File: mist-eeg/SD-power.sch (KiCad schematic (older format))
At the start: 14 parts, among them U8 TPS63070

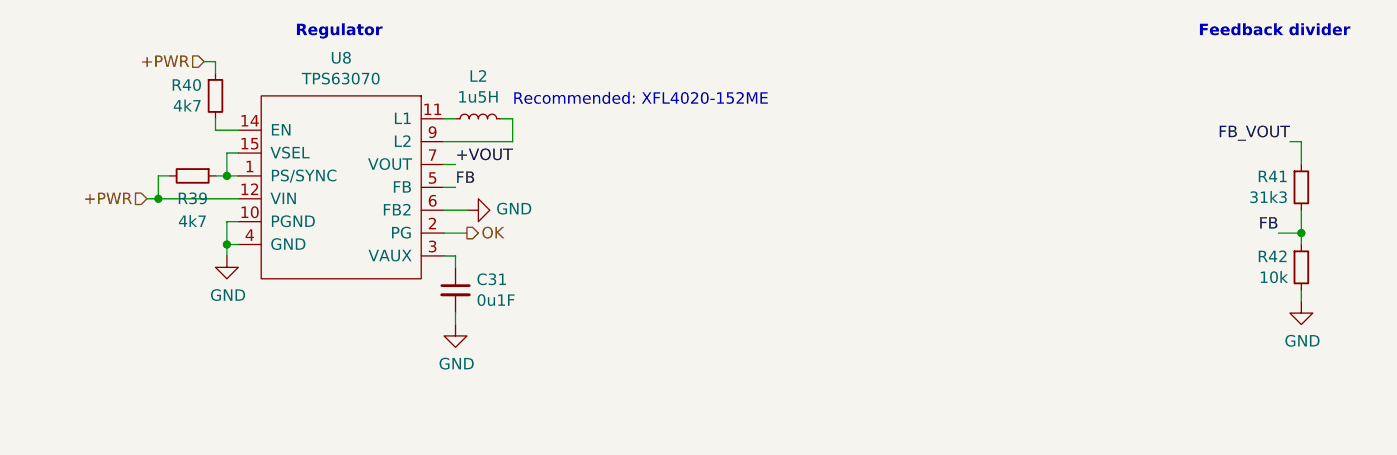
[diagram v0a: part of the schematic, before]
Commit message: Finish schematic and create interface specifications
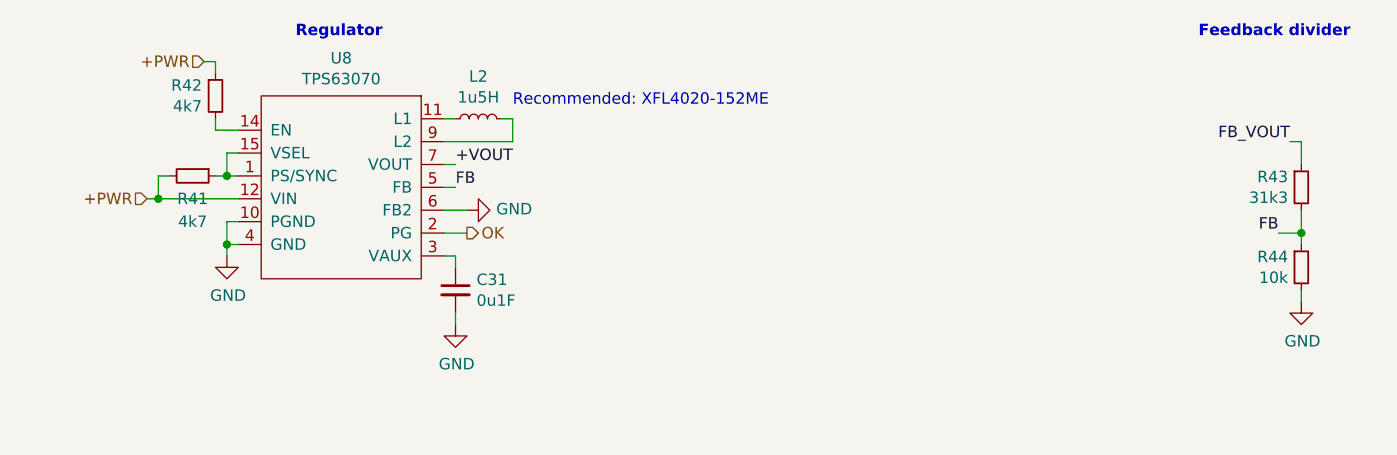
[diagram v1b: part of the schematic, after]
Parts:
- renumbered R39 to R41, R40 to R42, R41 to R43, R42 to R44
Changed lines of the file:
@@
 P 3750 2700
 AR Path="/609A79EB/60F89803/6135F6B6" Ref="R?"  Part="1"
-AR Path="/609A79EB/60FA92B1/6135F6B6" Ref="R39"  Part="1"
-F 0 "R39" V 3850 2700 50  0000 C CNN
+AR Path="/609A79EB/60FA92B1/6135F6B6" Ref="R41"  Part="1"
+F 0 "R41" V 3850 2700 50  0000 C CNN
 F 1 "4k7" V 3950 2700 50  0000 C CNN
 F 2 "Resistor_SMD:R_0201_0603Metric" H 3750 2700 50  0001 C CNN
@@
 P 8600 2750
 AR Path="/609A79EB/60F89803/6135F6F8" Ref="R?"  Part="1"
-AR Path="/609A79EB/60FA92B1/6135F6F8" Ref="R41"  Part="1"
-F 0 "R41" H 8542 2796 50  0000 R CNN
+AR Path="/609A79EB/60FA92B1/6135F6F8" Ref="R43"  Part="1"
+F 0 "R43" H 8542 2796 50  0000 R CNN
 F 1 "31k3" H 8542 2705 50  0000 R CNN
 F 2 "Resistor_SMD:R_0603_1608Metric" H 8600 2750 50  0001 C CNN
@@
 P 8600 3100
 AR Path="/609A79EB/60F89803/6135F6FE" Ref="R?"  Part="1"
-AR Path="/609A79EB/60FA92B1/6135F6FE" Ref="R42"  Part="1"
-F 0 "R42" H 8542 3146 50  0000 R CNN
+AR Path="/609A79EB/60FA92B1/6135F6FE" Ref="R44"  Part="1"
+F 0 "R44" H 8542 3146 50  0000 R CNN
 F 1 "10k" H 8542 3055 50  0000 R CNN
 F 2 "Resistor_SMD:R_0603_1608Metric" H 8600 3100 50  0001 C CNN
@@
 P 3850 2350
 AR Path="/609A79EB/60F89803/6135F719" Ref="R?"  Part="1"
-AR Path="/609A79EB/60FA92B1/6135F719" Ref="R40"  Part="1"
-F 0 "R40" H 3791 2396 50  0000 R CNN
+AR Path="/609A79EB/60FA92B1/6135F719" Ref="R42"  Part="1"
+F 0 "R42" H 3791 2396 50  0000 R CNN
 F 1 "4k7" H 3791 2305 50  0000 R CNN
 F 2 "Resistor_SMD:R_0201_0603Metric" H 3850 2350 50  0001 C CNN
@@
 P 2400 5100
 AR Path="/609A79EB/60F89803/6135F747" Ref="#PWR?"  Part="1"
-AR Path="/609A79EB/60FA92B1/6135F747" Ref="#PWR053"  Part="1"
-F 0 "#PWR053" H 2400 4850 50  0001 C CNN
+AR Path="/609A79EB/60FA92B1/6135F747" Ref="#PWR054"  Part="1"
+F 0 "#PWR054" H 2400 4850 50  0001 C CNN
 F 1 "GND" V 2405 4972 50  0000 R CNN
 F 2 "" H 2400 5100 50  0001 C CNN
@@
 P 6200 5200
 AR Path="/609A79EB/60F89803/6135F74D" Ref="#PWR?"  Part="1"
-AR Path="/609A79EB/60FA92B1/6135F74D" Ref="#PWR057"  Part="1"
-F 0 "#PWR057" H 6200 4950 50  0001 C CNN
+AR Path="/609A79EB/60FA92B1/6135F74D" Ref="#PWR058"  Part="1"
+F 0 "#PWR058" H 6200 4950 50  0001 C CNN
 F 1 "GND" H 6205 5027 50  0000 C CNN
 F 2 "" H 6200 5200 50  0001 C CNN
@@
 P 3900 3050
 AR Path="/609A79EB/60F89803/6135F753" Ref="#PWR?"  Part="1"
-AR Path="/609A79EB/60FA92B1/6135F753" Ref="#PWR054"  Part="1"
-F 0 "#PWR054" H 3900 2800 50  0001 C CNN
+AR Path="/609A79EB/60FA92B1/6135F753" Ref="#PWR055"  Part="1"
+F 0 "#PWR055" H 3900 2800 50  0001 C CNN
 F 1 "GND" H 3905 2877 50  0000 C CNN
 F 2 "" H 3900 3050 50  0001 C CNN
@@
 P 4900 3350
 AR Path="/609A79EB/60F89803/6135F759" Ref="#PWR?"  Part="1"
-AR Path="/609A79EB/60FA92B1/6135F759" Ref="#PWR055"  Part="1"
-F 0 "#PWR055" H 4900 3100 50  0001 C CNN
+AR Path="/609A79EB/60FA92B1/6135F759" Ref="#PWR056"  Part="1"
+F 0 "#PWR056" H 4900 3100 50  0001 C CNN
 F 1 "GND" H 4905 3177 50  0000 C CNN
 F 2 "" H 4900 3350 50  0001 C CNN
@@
 P 4950 2850
 AR Path="/609A79EB/60F89803/6135F75F" Ref="#PWR?"  Part="1"
-AR Path="/609A79EB/60FA92B1/6135F75F" Ref="#PWR056"  Part="1"
-F 0 "#PWR056" H 4950 2600 50  0001 C CNN
+AR Path="/609A79EB/60FA92B1/6135F75F" Ref="#PWR057"  Part="1"
+F 0 "#PWR057" H 4950 2600 50  0001 C CNN
 F 1 "GND" V 4955 2722 50  0000 R CNN
 F 2 "" H 4950 2850 50  0001 C CNN
@@
 P 8600 3250
 AR Path="/609A79EB/60F89803/6135F765" Ref="#PWR?"  Part="1"
-AR Path="/609A79EB/60FA92B1/6135F765" Ref="#PWR058"  Part="1"
-F 0 "#PWR058" H 8600 3000 50  0001 C CNN
+AR Path="/609A79EB/60FA92B1/6135F765" Ref="#PWR059"  Part="1"
+F 0 "#PWR059" H 8600 3000 50  0001 C CNN
 F 1 "GND" H 8605 3077 50  0000 C CNN
 F 2 "" H 8600 3250 50  0001 C CNN

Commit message: Advance routing
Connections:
- net +3V3 renamed +3V3_SD
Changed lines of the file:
@@
 $Descr USLetter 11000 8500
 encoding utf-8
-Sheet 6 12
+Sheet 5 11
 Title "Portiloop"
 Date "2021-06-07"
@@
 	6350 5000 6350 5150
 Text HLabel 6700 4650 2    50   Output ~ 0
-+3V3
++3V3_SD
 Wire Wire Line
 	6200 4650 6200 4700

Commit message: Validation & fabrication layer
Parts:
- removed R42: 4k7, Resistor_SMD:R_0201_0603Metric, symbol Device:R_Small
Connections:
- net ENA: now reaches U8.14 (EN)
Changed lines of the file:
@@
 Regulator
-$Comp
-L Device:R_Small R?
-U 1 1 6135F719
-P 3850 2350
-AR Path="/609A79EB/60F89803/6135F719" Ref="R?"  Part="1"
-AR Path="/609A79EB/60FA92B1/6135F719" Ref="R42"  Part="1"
-F 0 "R42" H 3791 2396 50  0000 R CNN
-F 1 "4k7" H 3791 2305 50  0000 R CNN
-F 2 "Resistor_SMD:R_0201_0603Metric" H 3850 2350 50  0001 C CNN
-F 3 "~" H 3850 2350 50  0001 C CNN
-	1    3850 2350
-	1    0    0    -1
-$EndComp
-Wire Wire Line
-	3850 2450 3850 2500
-Wire Wire Line
-	3850 2500 3950 2500
-Text HLabel 3800 2200 0    50   Input ~ 0
-+PWR
-Wire Wire Line
-	3800 2200 3850 2200
-Wire Wire Line
-	3850 2200 3850 2250
 $Comp
 L Device:C_Small C?
@@
 	1    0    0    -1
 $EndComp
+Text HLabel 3900 2500 0    50   Input ~ 0
+ENA
+Wire Wire Line
+	3900 2500 3950 2500
 $EndSCHEMATC

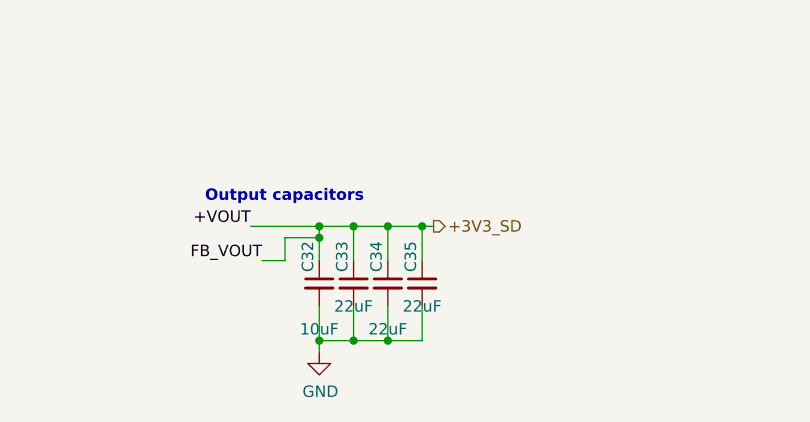
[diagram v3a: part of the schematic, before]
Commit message: Update footprints based upon piece availability & generate manufacturing files
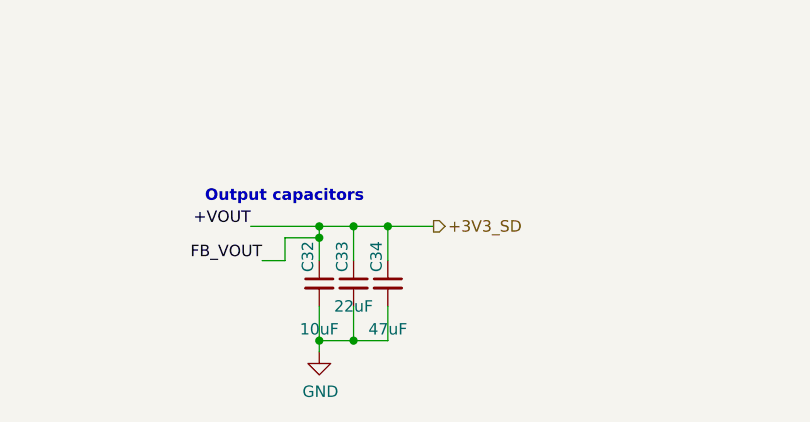
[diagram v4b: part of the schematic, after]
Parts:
- removed C35: 22uF, Capacitor_SMD:C_0603_1608Metric, symbol Device:C_Small
- C34: value 22uF -> 47uF; footprint Capacitor_SMD:C_0603_1608Metric -> Capacitor_SMD:C_1210_3225Metric
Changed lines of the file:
@@
 Wire Wire Line
 	6500 4650 6500 4800
-Wire Wire Line
-	6650 4650 6500 4650
-Wire Wire Line
-	6650 4650 6700 4650
-Connection ~ 6650 4650
-Wire Wire Line
-	6650 4650 6650 4800
-$Comp
-L Device:C_Small C?
-U 1 1 6135F734
-P 6650 4900
-AR Path="/609A79EB/60F89803/6135F734" Ref="C?"  Part="1"
-AR Path="/609A79EB/60FA92B1/6135F734" Ref="C35"  Part="1"
-F 0 "C35" V 6600 4950 50  0000 L CNN
-F 1 "22uF" H 6650 4800 50  0000 C CNN
-F 2 "Capacitor_SMD:C_0603_1608Metric" H 6650 4900 50  0001 C CNN
-F 3 "~" H 6650 4900 50  0001 C CNN
-	1    6650 4900
-	1    0    0    -1
-$EndComp
 $Comp
 L Device:C_Small C?
@@
 AR Path="/609A79EB/60FA92B1/6135F73A" Ref="C34"  Part="1"
 F 0 "C34" V 6450 4950 50  0000 L CNN
-F 1 "22uF" H 6500 4700 50  0000 C CNN
-F 2 "Capacitor_SMD:C_0603_1608Metric" H 6500 4900 50  0001 C CNN
+F 1 "47uF" H 6500 4700 50  0000 C CNN
+F 2 "Capacitor_SMD:C_1210_3225Metric" H 6500 4900 50  0001 C CNN
 F 3 "~" H 6500 4900 50  0001 C CNN
 	1    6500 4900
@@
 $EndComp
 Wire Wire Line
-	6650 5000 6650 5150
-Wire Wire Line
 	6500 5000 6500 5150
-Wire Wire Line
-	6500 5150 6650 5150
-Connection ~ 6500 5150
 Connection ~ 6350 5150
 Wire Wire Line
@@
 Wire Wire Line
 	3900 2500 3950 2500
+Wire Wire Line
+	6500 4650 6700 4650
 $EndSCHEMATC

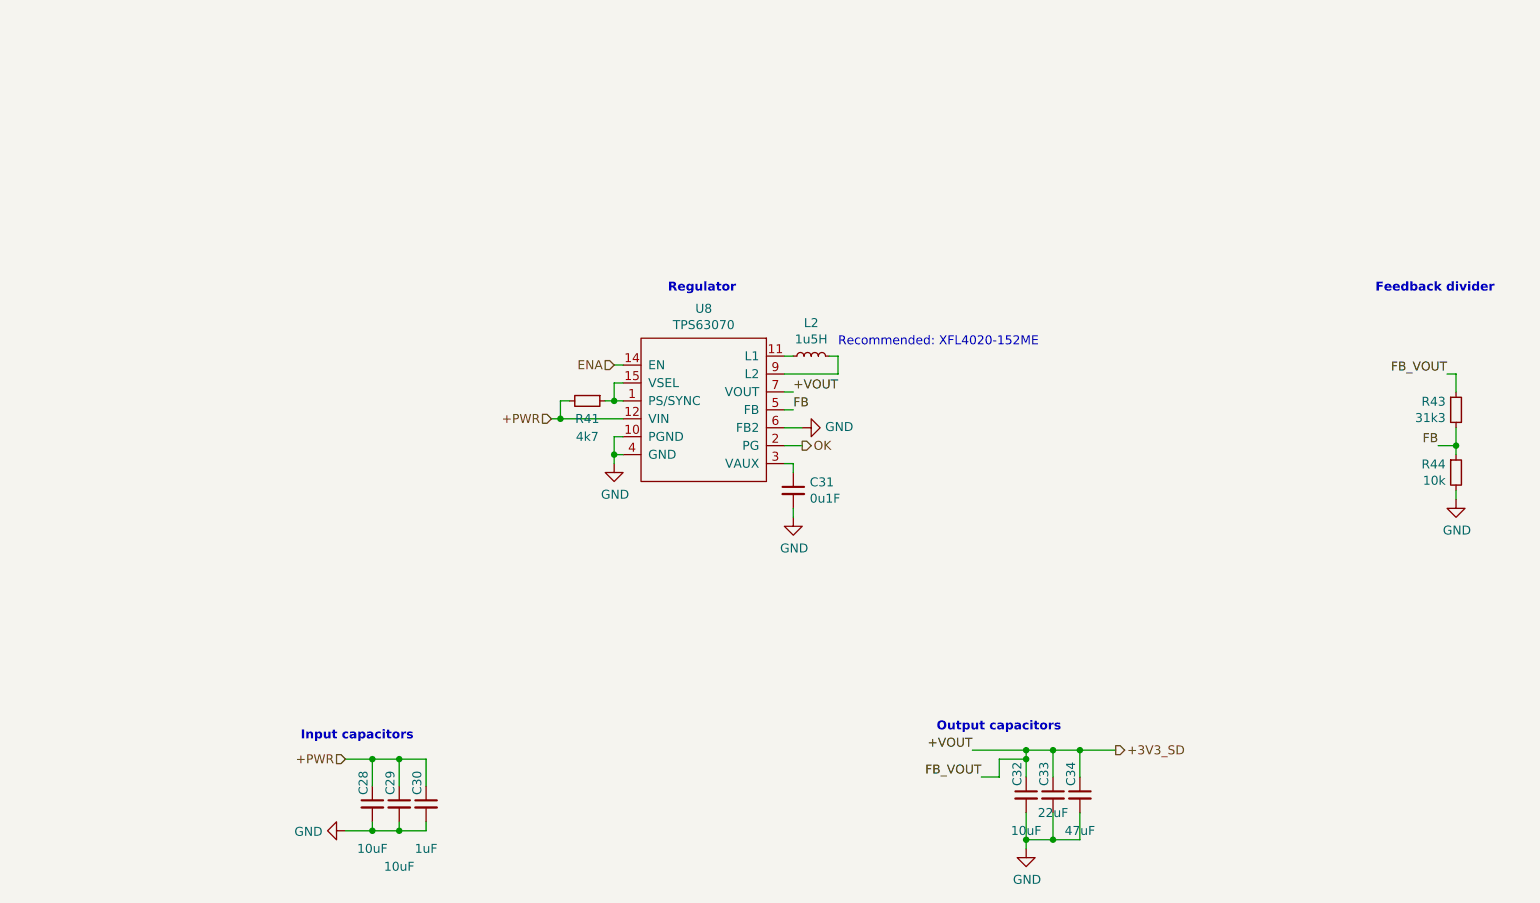
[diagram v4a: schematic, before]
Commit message: Change buckboost regulator used
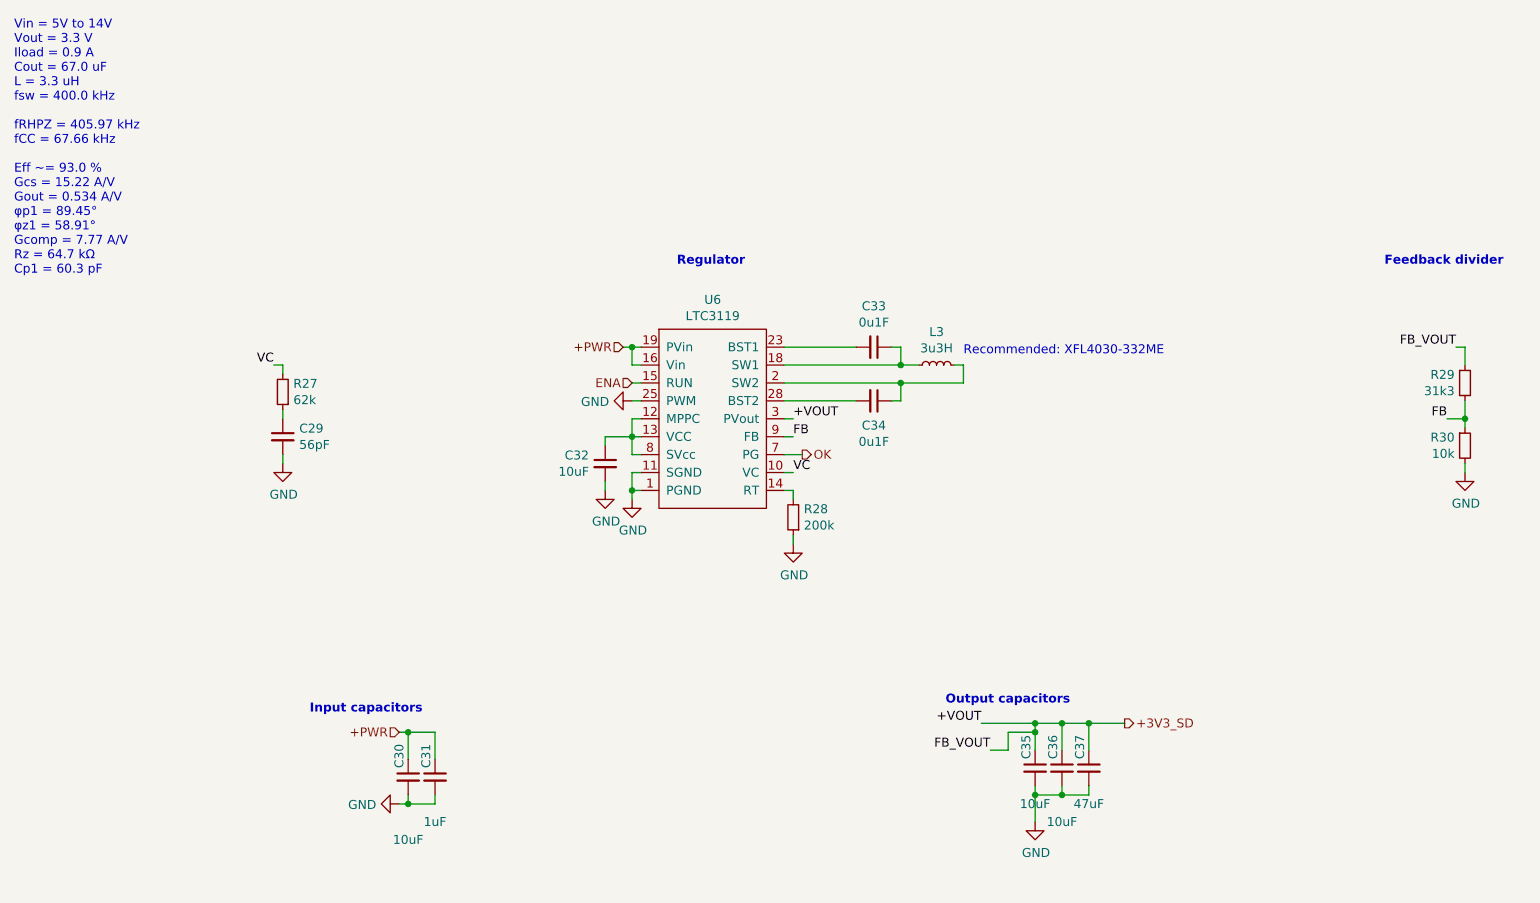
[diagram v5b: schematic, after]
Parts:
- removed U8: TPS63070, mist-eeg:TPS630702RNMR, symbol components:TPS63070
- added C32: 10uF, Capacitor_SMD:C_0603_1608Metric, symbol Device:C_Small
- added C34: 0u1F, Capacitor_SMD:C_0201_0603Metric, symbol Device:C_Small
- added R28: 200k, Resistor_SMD:R_0201_0603Metric, symbol Device:R_Small
- added U6: LTC3119, Package_DFN_QFN:QFN-28-1EP_4x5mm_P0.5mm_EP2.65x3.65mm, symbol components:LTC3119
- C29: renamed from C31; value 0u1F -> 56pF
- C33: value 22uF -> 0u1F; footprint Capacitor_SMD:C_0603_1608Metric -> Capacitor_SMD:C_0201_0603Metric
- L3: renamed from L2; value 1u5H -> 3u3H
- R27: renamed from R41; value 4k7 -> 62k
- renumbered C29 to C30, C30 to C31, C32 to C35, C28 to C36, C34 to C37, R43 to R29, R44 to R30
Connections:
- net +3V3_SD: now also C36.1, U6.3 (PVout), U6.4 (PVout); no longer C33.1
- net +PWR: now also U6.16 (Vin), U6.19 (PVin), U6.20 (PVin); no longer C36.1, R27.2
- net ENA: now also U6.15 (RUN)
- net FB: now also U6.9 (FB)
- net GND: now also C32.2, R28.1, U6.1 (PGND), U6.11 (SGND), U6.17 (PGND), U6.22 (PGND), U6.25 (PWM), U6.29 (PGND), U6.6 (PGND); no longer C33.2
- net OK: now also U6.7 (PG)
- net at R27.1: now also C29.1
- net at L3.1: now also C33.1, U6.18 (SW1), U6.21 (SW1)
- net at L3.2: now also C34.1, U6.2 (SW2), U6.5 (SW2)
- new net: R28.2, U6.14 (RT)
- new net: C32.1, U6.12 (MPPC), U6.13 (VCC), U6.8 (SVcc)
- new net: C33.2, U6.23 (BST1)
- new net: C34.2, U6.28 (BST2)
- new net VC: R27.2, U6.10 (VC)
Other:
- note added: "Recommended: XFL4030-332ME"
- note added: "Vin = 5V to 14V\nVout = 3.3 V\nIload = 0.9 A\nCout = 67.0 uF\nL = 3.3 uH\nfsw = 400.0 kHz\n\nfRHPZ = 405.97 kHz\nfCC = 67.66 kHz\n\nEff ~~= 93.0 %\nGcs = 15.22 A/V\nGout = 0.534 A/V\nφp1 = 89.45°\nφz1 = 58.91°\nGcomp = 7.77 A/V\nRz = 64.7 kΩ\nCp1 = 60.3 pF"
- note removed: "Recommended: XFL4020-152ME"
- moved on the sheet: C29, C30, C31, C35, C36, C37, L3, R27, R29, R30
